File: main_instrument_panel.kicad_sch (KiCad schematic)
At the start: 22 parts

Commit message: Proof reading and snagging updates
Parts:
- TB6: renamed from TB5; symbol Connector:Screw_Terminal_01x12 -> Connector:Screw_Terminal_01x10
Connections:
- net GND: no longer TB6.11 (Pin_11), TB6.12 (Pin_12)
- net TB6/8: now reaches J?.2
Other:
- note added: "Instrument Module Earth Bus"
- note added: "SmartAss Speaking ASI Control Panel"
- note removed: "SmartAss Speaking ASI"
- title: (none) -> Main Instrument Panel
- moved on the sheet: J?

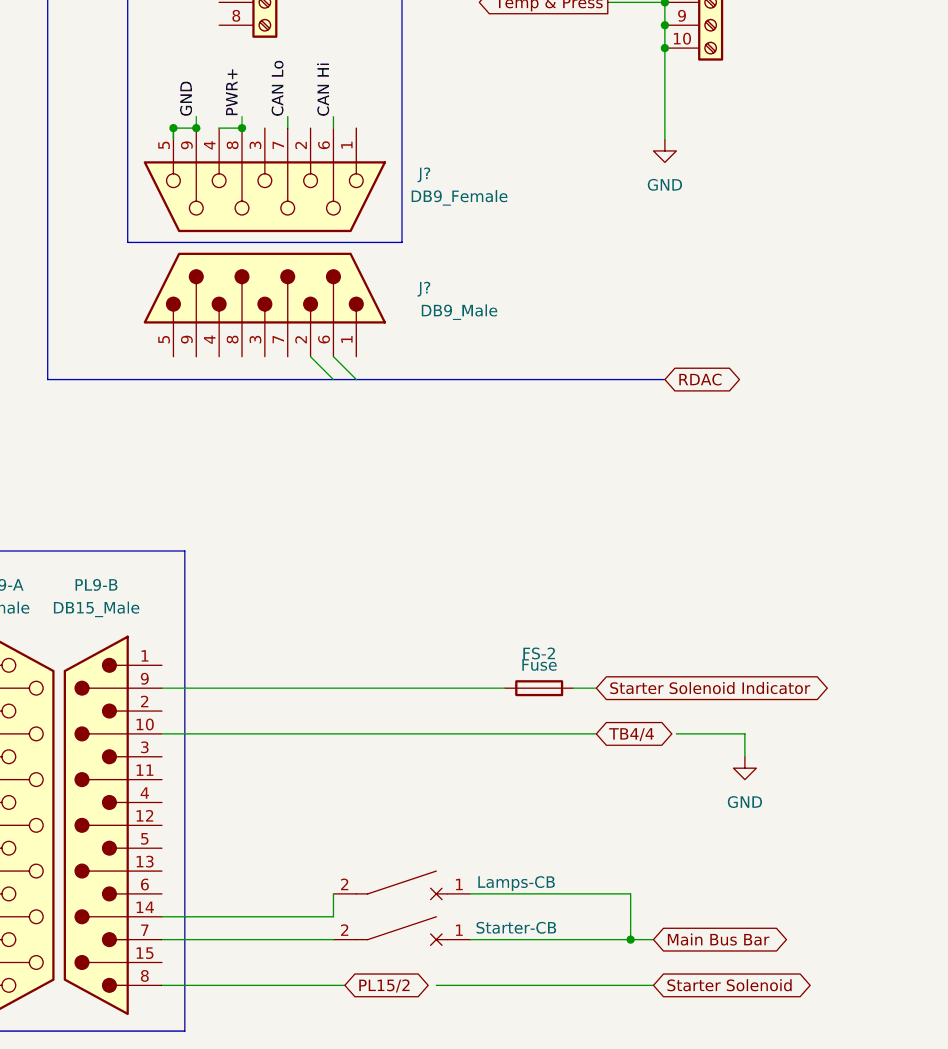
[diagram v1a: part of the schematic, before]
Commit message: Updates from manual validation
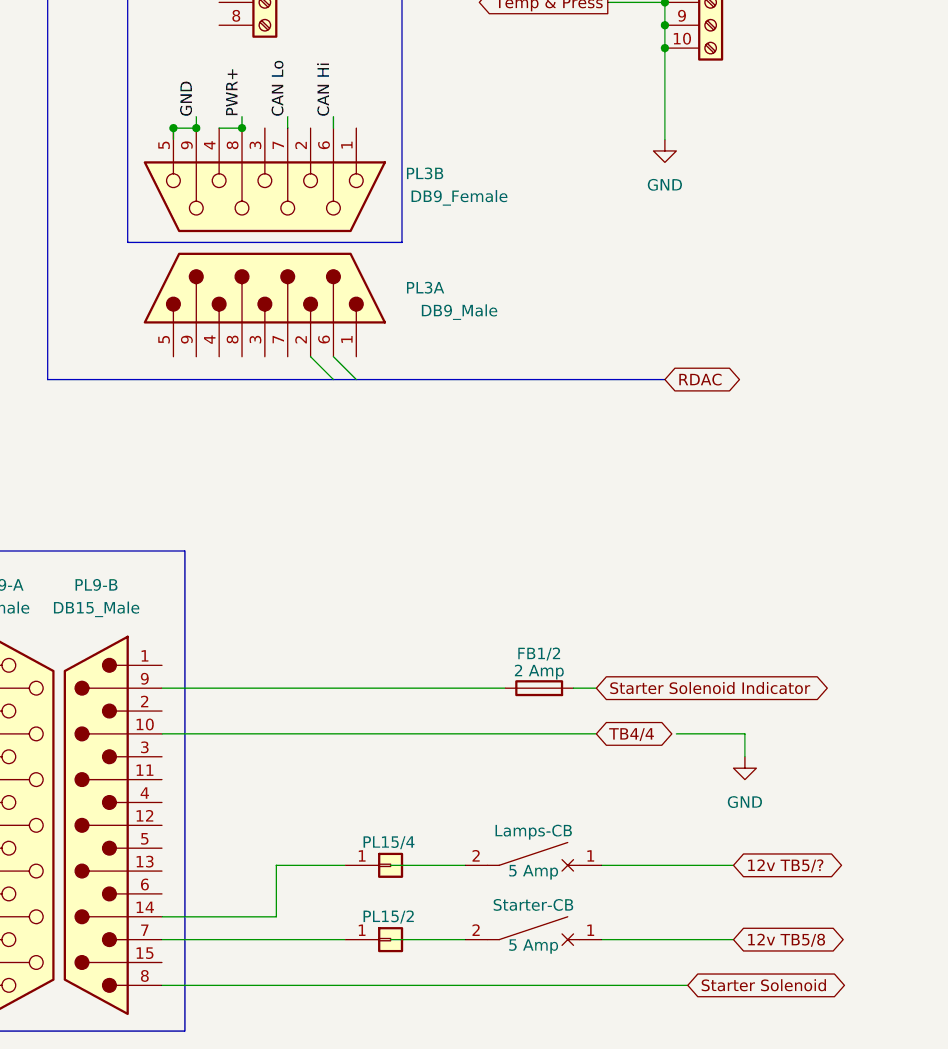
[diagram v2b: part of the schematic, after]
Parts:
- added PL15/2, PL15/4: Conn_01x01, symbol Connector_Generic:Conn_01x01
- FB1/2: renamed from FS-2; Rating (none) -> 2 Amp
- Lamps-CB, Starter-CB: Rating (none) -> 5 Amp
- gave numbers to parts that had none: 2
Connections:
- net PL15/2 is gone; now on net Starter Solenoid: PL9-B.8
- net at Lamps-CB.2: no longer PL9-B.14 (P14)
- net at PL9-B.7: now also PL15/2.1 (Pin_1); no longer Starter-CB.2
- net Main Bus Bar renamed 12v TB5/8
- net 12v TB5/8: no longer Lamps-CB.1
- new net: PL15/4.1 (Pin_1), PL9-B.14 (P14)
- new net 12v TB5/?: Lamps-CB.1
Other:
- moved on the sheet: Lamps-CB, Starter-CB
